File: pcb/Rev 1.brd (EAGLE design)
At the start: 76.8 x 76.8 mm, 248 parts, among them J1 3220-10-0100-00, J2 10118194-0001LF, J3 B2B-PH-K-S(LF)(SN), Q1 MMBT3904,215MMBT3904,215, Q10 MMBT3904,215MMBT3904,215, Q11 MMBT3904,215MMBT3904,215, Q12 MMBT3904,215MMBT3904,215, Q13 MMBT3904,215MMBT3904,215, Q14 MMBT3904,215MMBT3904,215, Q15 MMBT3904,215MMBT3904,215, Q16 TEFT4300, Q17 TEFT4300, Q18 TEFT4300, Q19 TEFT4300, Q2 MMBT3904,215MMBT3904,215, Q20 MMBT3904,215MMBT3904,215, Q21 MMBT3904,215MMBT3904,215, Q22 MMBT3904,215MMBT3904,215, Q23 MMBT3904,215MMBT3904,215, Q24 TEFT4300, Q25 TEFT4300, Q26 TEFT4300, Q27 TEFT4300, Q28 SI7157DP, Q29 SI7157DP, Q3 MMBT3904,215MMBT3904,215, Q30 MMBT3906, Q31 MMBT3906, Q32 SI7157DP, Q33 MMBT3906, Q34 MMBT3906, Q4 MMBT3904,215MMBT3904,215, Q5 MMBT3904,215MMBT3904,215, Q6 MMBT3904,215MMBT3904,215, Q7 MMBT3904,215MMBT3904,215, Q8 MMBT3904,215MMBT3904,215, Q9 MMBT3904,215MMBT3904,215, SW1 210-6MS, U1 ATSAMD21G18A-MU, U10 DRV8871, U2 AP3441, U3 TPS61089, U4 BNO055, U5 MCP73811, U7 DRV8871, U8 DRV8871, U9 DRV8871

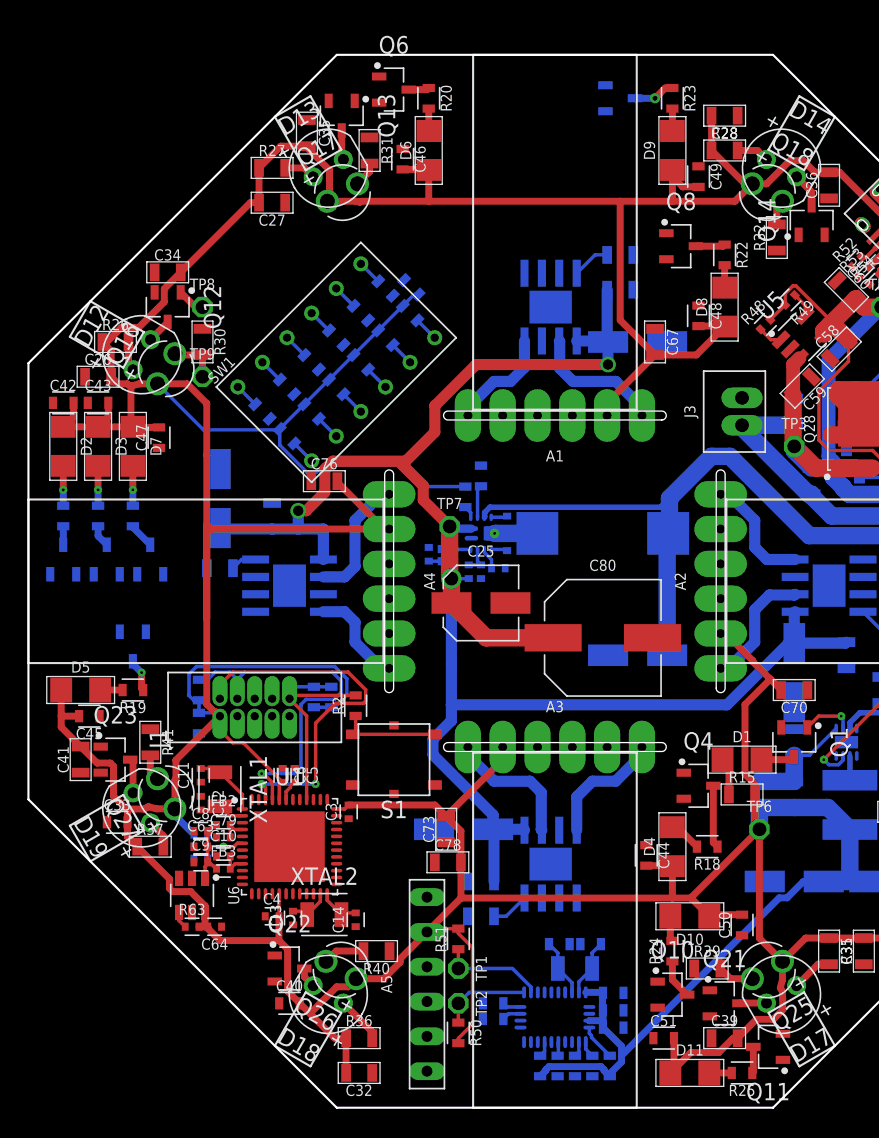
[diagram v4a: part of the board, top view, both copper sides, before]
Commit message: Removed the DIP switches and some LEDs
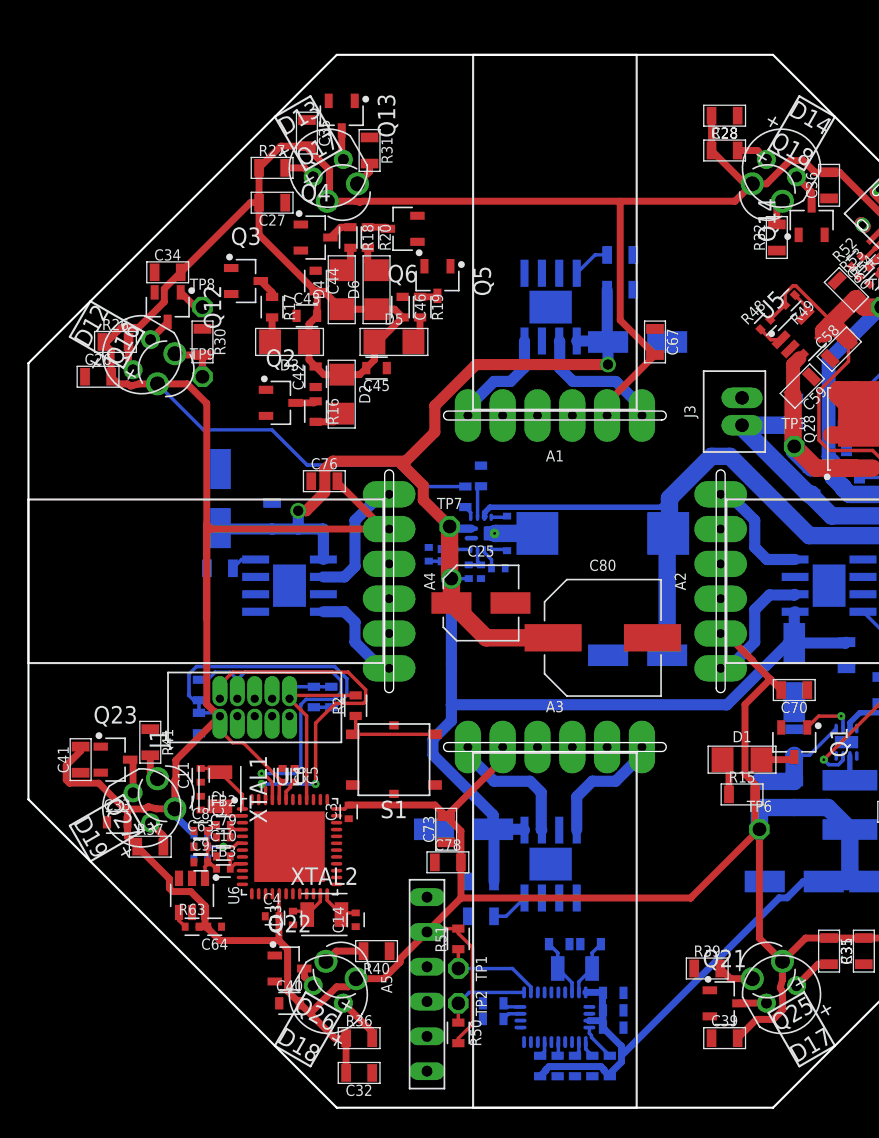
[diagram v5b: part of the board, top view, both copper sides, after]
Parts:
- removed C47, C48, C49, C50, C51: 1uF, Micromouse 2020:0603
- removed C77: 0.1uF, Micromouse 2020:0603
- removed D10, D11, D7, D8, D9: LED1206, Micromouse 2020:1206
- removed Q10, Q11, Q7, Q8, Q9: MMBT3904,215MMBT3904,215, Micromouse 2020:SOT95P230X110-3
- removed R21, R22, R23, R24, R25: 30R, Micromouse 2020:0603
- removed R71, R72, R73, R74, R75, R76: 10k, Micromouse 2020:0603
- removed R81, R82, R83, R84, R85, R86: 470k, Micromouse 2020:0603
- removed SW1: 210-6MS, Micromouse 2020:210-6MS
- moved R18 51.5 mm to (23.5, 63.5), turned to 270 degrees
- moved Q4 48.8 mm to (21.0, 63.5)
- moved C44 48.4 mm to (21.0, 60.3)
- moved D4 47.3 mm to (22.9, 59.7)
- moved R19 34.9 mm to (28.6, 58.4), turned to 270 degrees
- moved Q5 34.7 mm to (29.8, 60.3), flipped to the top
- moved D5 34.2 mm to (26.7, 55.9)
- moved C45 32.9 mm to (25.4, 54.0)
- moved Q3 22.7 mm to (15.9, 60.3), flipped to the top, turned to 0 degrees
- moved D2 20.7 mm to (22.9, 52.1)
- moved R16 19.9 mm to (21.0, 50.8), flipped to the top, turned to 270 degrees
- moved R17 19.8 mm to (17.8, 58.4), flipped to the top, turned to 270 degrees
- moved Q2 19.6 mm to (18.4, 51.4), flipped to the top, turned to 0 degrees
- moved C42 18.5 mm to (21.0, 53.3), turned to 90 degrees
- moved C43 16.5 mm to (20.3, 57.8)
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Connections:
- removed net LED5: Q7.1
- removed net LED6: Q8.1
- removed net LED7: Q9.1
- removed net LED8: Q10.1
- removed net LED9: Q11.1
- removed net N$100: R73.2, SW1.P9
- removed net N$101: R74.2, SW1.P10
- removed net N$102: R75.2, SW1.P11
- removed net N$103: R76.2, SW1.P12
- removed net N$30: Q7.3, R21.1
- removed net N$31: Q8.3, R22.1
- removed net N$32: Q9.3, R23.1
- removed net N$33: Q10.3, R24.1
- removed net N$34: Q11.3, R25.1
- removed net N$35: D7.2, R21.2
- removed net N$36: D8.2, R22.2
- removed net N$37: D9.2, R23.2
- removed net N$38: D10.2, R24.2
- removed net N$39: D11.2, R25.2
- removed net N$98: R71.2, SW1.P7
- removed net N$99: R72.2, SW1.P8
- removed net SW0: R86.1, SW1.P1
- removed net SW1: R85.1, SW1.P2
- removed net SW2: R84.1, SW1.P3
- removed net SW3: R83.1, SW1.P4
- removed net SW4: R82.1, SW1.P5
- removed net SW5: R81.1, SW1.P6
- net +3V3: no longer C47.2, C48.2, C49.2, C50.2, C51.2, C77.2, D10.1, D11.1, D7.1, D8.1, D9.1, R81.2, R82.2, R83.2, R84.2, R85.2, R86.2
- net GND: no longer C47.1, C48.1, C49.1, C50.1, C51.1, C77.1, Q10.2, Q11.2, Q7.2, Q8.2, Q9.2, R71.1, R72.1, R73.1, R74.1, R75.1, R76.1
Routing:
- net +3V3: track 540.2 -> 503.0 mm
- net N$32: track 3.04 -> 0.00 mm, vias 1 -> 0
- net N$35: track 2.91 -> 0.00 mm, vias 1 -> 0
- net N$33: track 2.87 -> 0.00 mm
- net N$22: track 4.57 -> 1.77 mm
- net N$31: track 2.14 -> 0.00 mm
- net N$34: track 1.94 -> 0.00 mm
- net N$30: track 1.87 -> 0.00 mm
- net N$38: track 1.85 -> 0.00 mm
- net SW1: track 1.79 -> 0.00 mm
- net N$100: track 1.79 -> 0.00 mm
- net N$99: track 1.79 -> 0.00 mm
- net N$98: track 1.79 -> 0.00 mm
- net SW4: track 1.79 -> 0.00 mm
- net N$102: track 1.79 -> 0.00 mm
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- added copper zone on layer 1, net +3V3

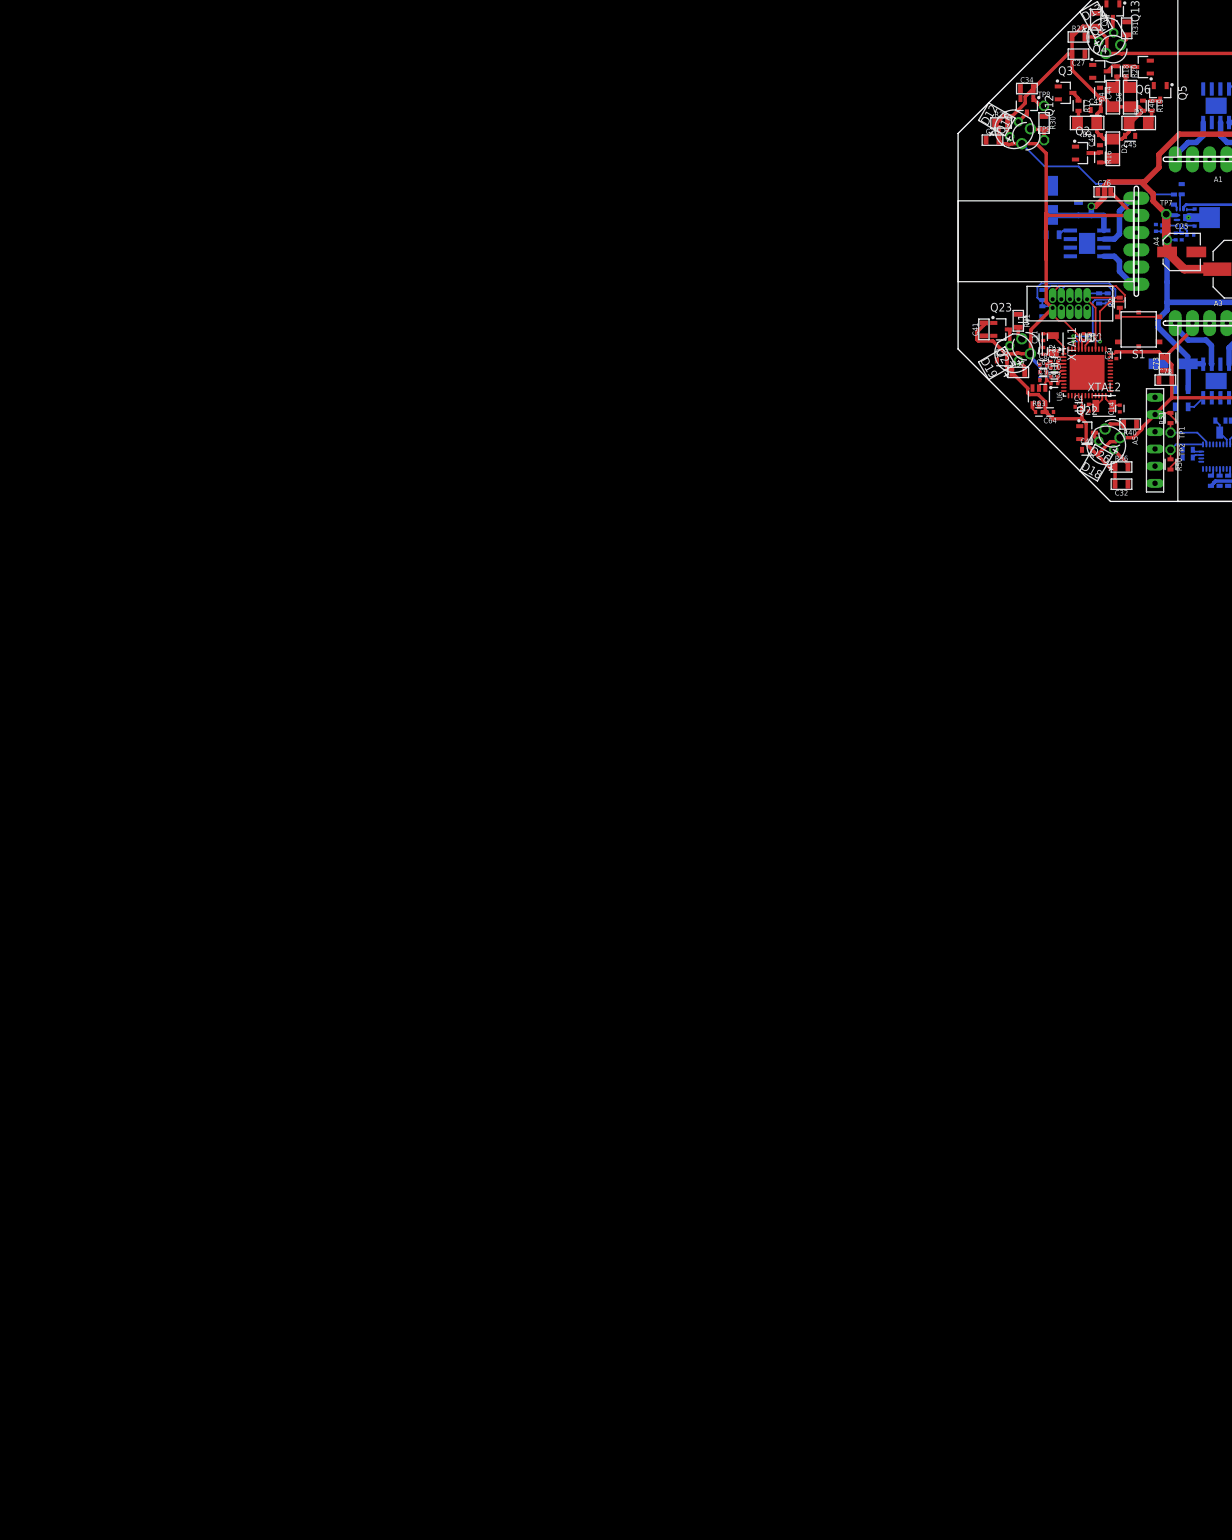
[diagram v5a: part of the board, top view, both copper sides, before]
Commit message: Added IO expanders
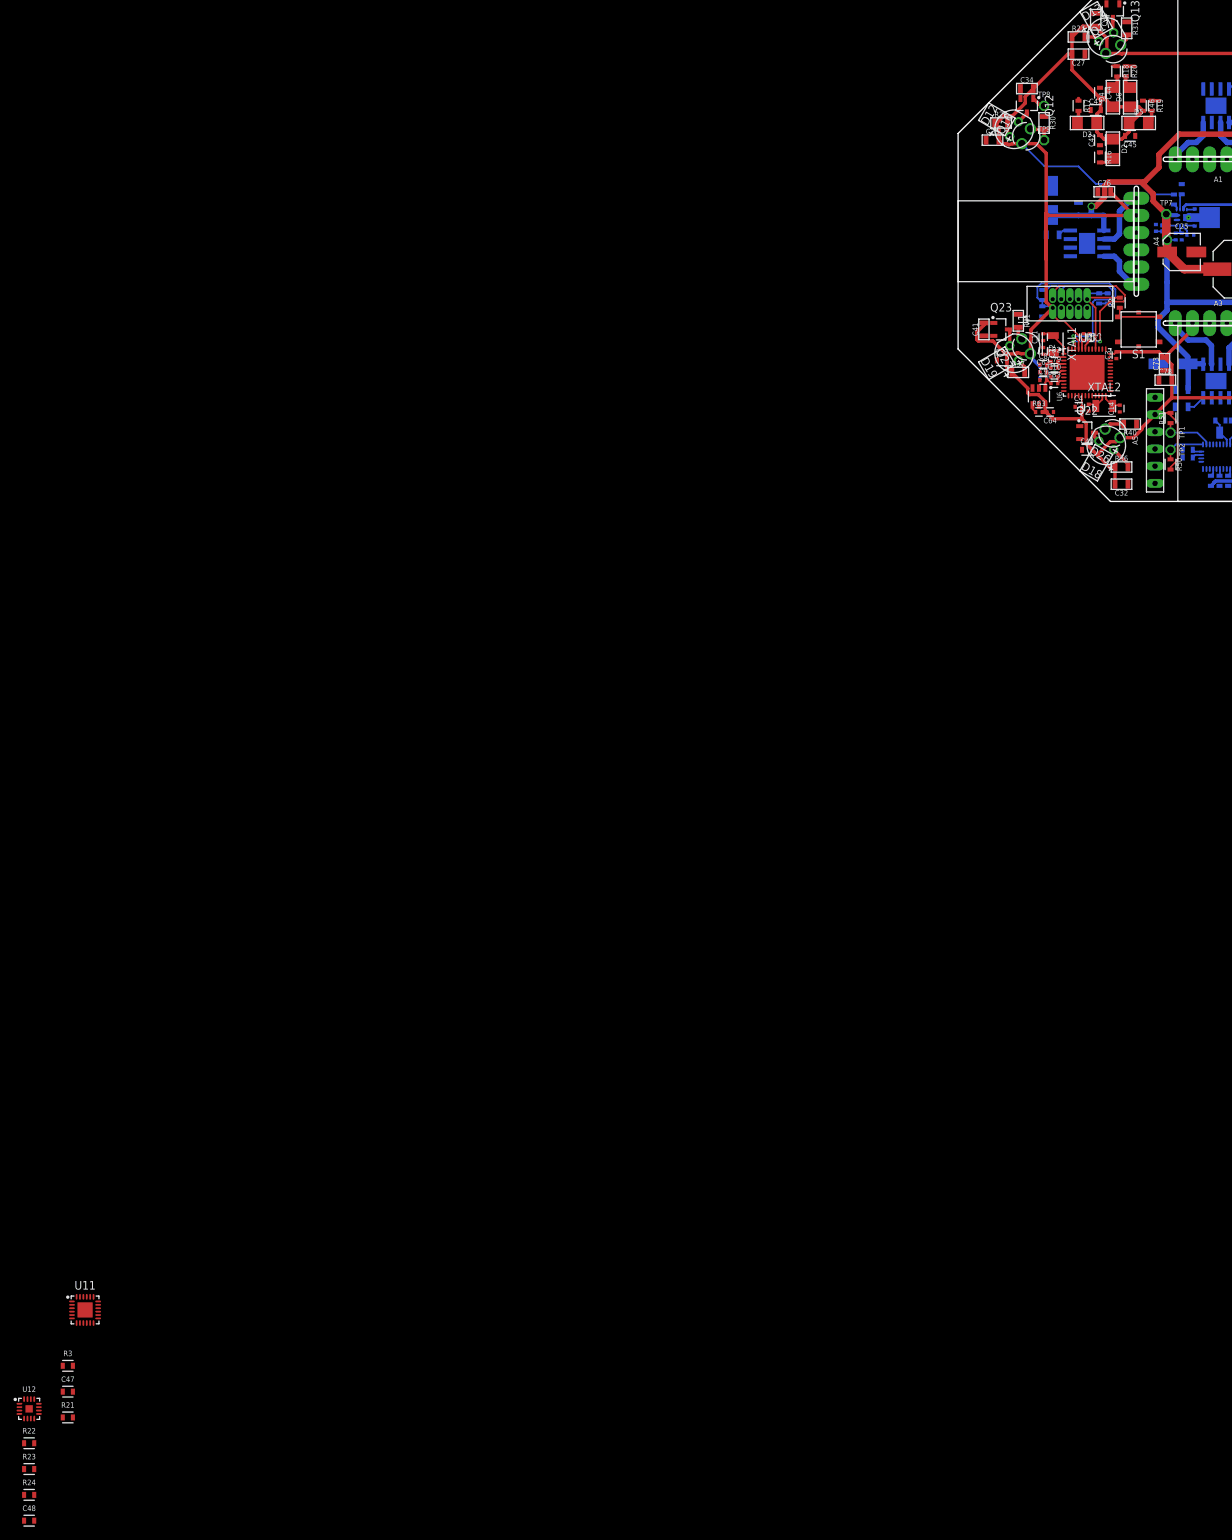
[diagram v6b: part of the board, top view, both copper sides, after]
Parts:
- removed Q2, Q3, Q4, Q5, Q6: MMBT3904,215MMBT3904,215, Micromouse 2020:SOT95P230X110-3
- added C47, C48: 0.1uF, Micromouse 2020:0603
- added R21, R22, R23, R24, R3: 10k, Micromouse 2020:0603
- added U11: PCAL6416A, Micromouse 2020:PCAL6416A
- added U12: MAX7315, Micromouse 2020:MAX7315
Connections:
- removed net N$20: Q2.3, R16.1
- removed net N$24: Q6.3, R20.1
- new net N$31: R3.1, U11.24
- new net N$32: R21.2, U11.18
- net +3V3: now also C47.2, C48.2, R3.2, U11.21, U11.23, U12.14
- net GND: now also C47.1, C48.1, R21.1, R22.1, R23.1, R24.1, U11.25, U11.9, U12.17, U12.6; no longer Q2.2, Q3.2, Q4.2, Q5.2, Q6.2
- net IR1: now also U11.10
- net IR2: now also U11.11
- net IR3: now also U11.12
- net IR4: now also U11.13
- net IR5: now also U11.14
- net IR6: now also U11.15
- net IR7: now also U11.16
- net IR8: now also U11.17
- net LED0: now also R16.1, U11.1; no longer Q2.1
- net LED1: now also R17.1, U11.2; no longer Q3.1
- net LED2: now also R18.1, U11.3; no longer Q4.1
- net LED3: now also R19.1, U11.4; no longer Q5.1
- net LED4: now also R20.1, U11.5; no longer Q6.1
- net MOTOR_1A: now also U12.2
- net MOTOR_1B: now also U12.3
- net MOTOR_2A: now also U12.4
- net MOTOR_2B: now also U12.5
- net MOTOR_3A: now also U12.7
- net MOTOR_3B: now also U12.8
- net MOTOR_4A: now also U12.9
- net MOTOR_4B: now also U12.10
- net N$21: now also R22.2, U12.1; no longer Q3.3, R17.1
- net N$22: now also R23.2, U12.16; no longer Q4.3, R18.1
- net N$23: now also R24.2, U12.15; no longer Q5.3, R19.1
- net SCL: now also U11.19, U12.12
- net SDA: now also U11.20, U12.13
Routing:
- net N$22: track 1.77 -> 0.00 mm
- net N$24: track 1.51 -> 0.00 mm
- net N$20: track 1.51 -> 0.00 mm
- net N$21: track 1.50 -> 0.00 mm
- net LED4: track 0.00 -> 1.35 mm
- net N$23: track 1.30 -> 0.00 mm
- net LED3: track 0.00 -> 1.19 mm
- net LED2: track 0.00 -> 0.71 mm
